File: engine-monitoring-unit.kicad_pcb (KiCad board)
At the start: 2 copper layers, 65.5 x 39.5 mm, 57 parts, among them J1 SW Debug, J2 Supply, J3 Oil Temperature, J4 Air Temperature, J5 Wheel Speed, J7 Inductive Sensor Wire, Q2 MMBT3904, SW1 KEY, SW2 BOOT, SW3 RST, U1 LMR16006XDDCR, U2 STM32F411CEU6, Y1 HSE, Y2 LSE

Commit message: Updated Page Settings, Board Stackup and Constraints
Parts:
- moved D6 109.9 mm to (149.7, 135.2)
- moved C1 109.9 mm to (127.9, 122.2)
- moved C10 109.9 mm to (132.3, 127.2)
- moved C11 109.9 mm to (132.3, 129.7)
- moved C12 109.9 mm to (132.3, 132.3)
- moved C14 109.9 mm to (132.3, 137.3)
- moved C15 109.9 mm to (136.6, 122.2)
- moved C16 109.9 mm to (136.6, 124.7)
- moved C17 109.9 mm to (136.6, 127.2)
- moved C2 109.9 mm to (127.9, 124.7)
- moved C3 109.9 mm to (127.9, 127.2)
- moved C4 109.9 mm to (127.9, 129.7)
- moved C5 109.9 mm to (127.9, 132.3)
- moved C7 109.9 mm to (127.9, 137.3)
- moved C8 109.9 mm to (132.3, 122.2)
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- renumbered D5 to D4, D4 to D5, D7 to D6, D6 to D7, J7 to J6, Q2 to Q1, R16 to R15, R15 to R16
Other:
- board size 65.5 x 39.5 mm -> 70 x 50 mm
- copper layers 2 -> 4

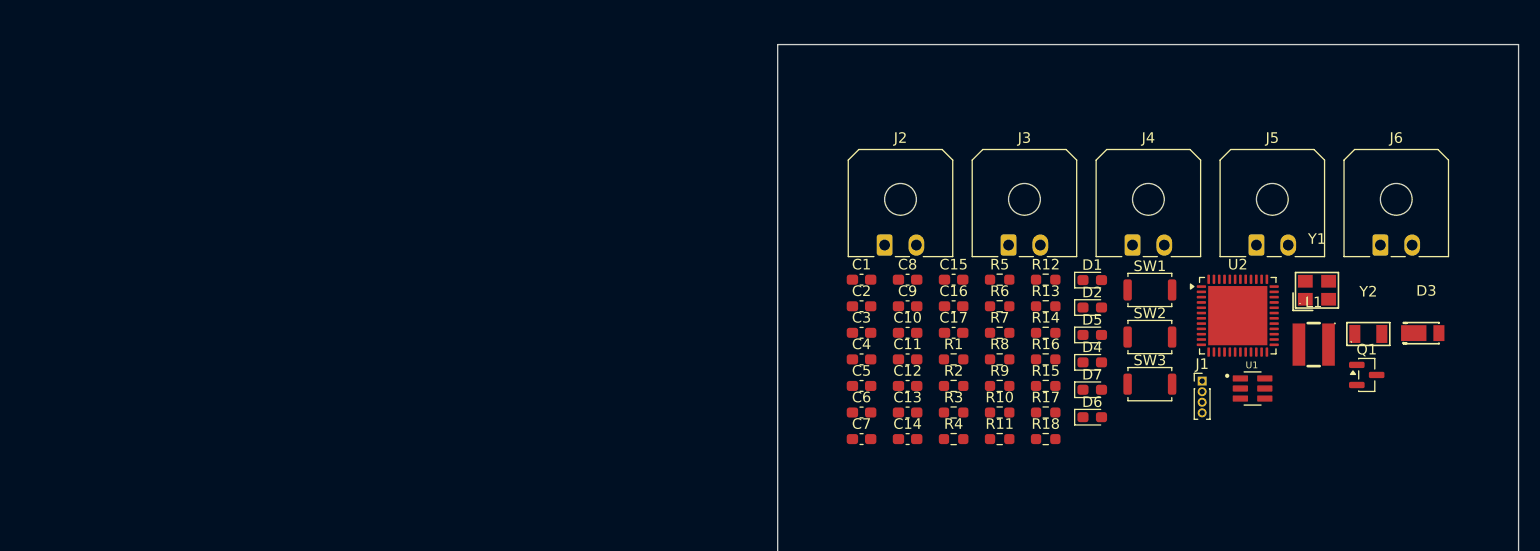
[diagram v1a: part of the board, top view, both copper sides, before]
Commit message: Layed out regulator circuit
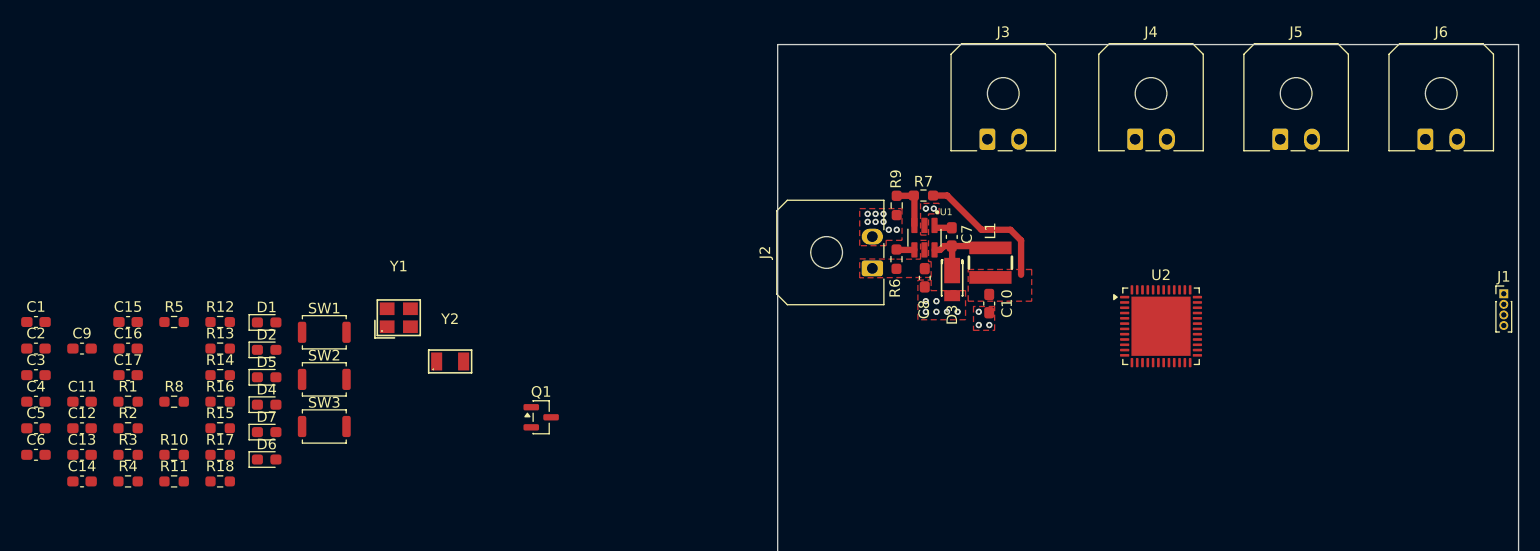
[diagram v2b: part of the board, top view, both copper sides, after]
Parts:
- moved Y2 86.8 mm to (89.1, 129.9)
- moved Y1 86.8 mm to (84.2, 125.8)
- moved C1 78.1 mm to (49.9, 126.2)
- moved C11 78.1 mm to (54.3, 133.7)
- moved C12 78.1 mm to (54.3, 136.3)
- moved C13 78.1 mm to (54.3, 138.8)
- moved C14 78.1 mm to (54.3, 141.3)
- moved C15 78.1 mm to (58.6, 126.2)
- moved C16 78.1 mm to (58.6, 128.7)
- moved C17 78.1 mm to (58.6, 131.2)
- moved C2 78.1 mm to (49.9, 128.7)
- moved C3 78.1 mm to (49.9, 131.2)
- moved C4 78.1 mm to (49.9, 133.7)
- moved C5 78.1 mm to (49.9, 136.3)
- moved C6 78.1 mm to (49.9, 138.8)
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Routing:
- net +3.3V: track 0.00 -> 13.3 mm
- net Net-(D3-K): track 0.00 -> 7.54 mm
- net Net-(U1-FB): track 0.00 -> 4.36 mm
- net Net-(U1-SHDN): track 0.00 -> 1.66 mm
- net Net-(U1-CB): track 0.00 -> 1.41 mm
- net GND: vias 0 -> 19
- added copper zone on F.Cu, net +3.3V
- added copper zone on F.Cu, net GND
- added copper zone on In1.Cu, net GND
- added copper zone on In2.Cu, net GND
- added copper zone on F.Cu, net VIN

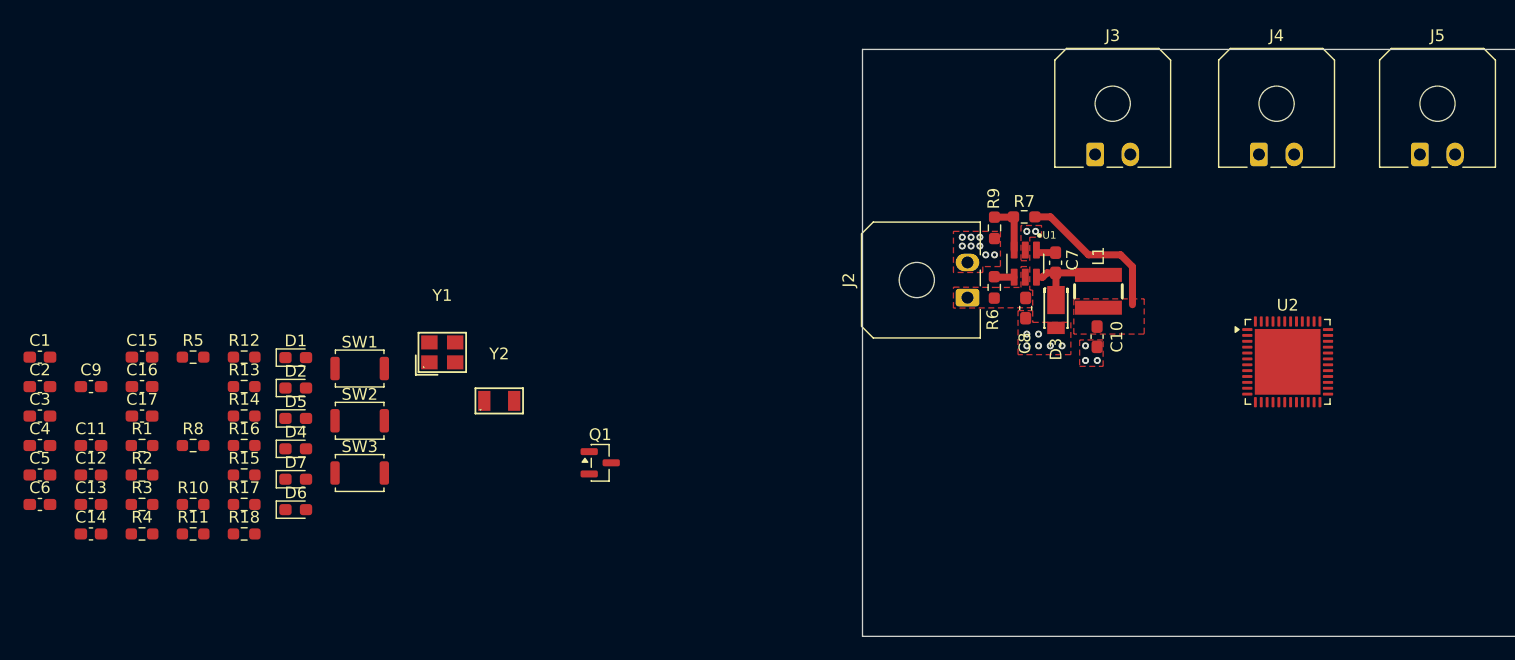
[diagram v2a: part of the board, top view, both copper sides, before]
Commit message: Layed out decoupling caps, connectors and switches
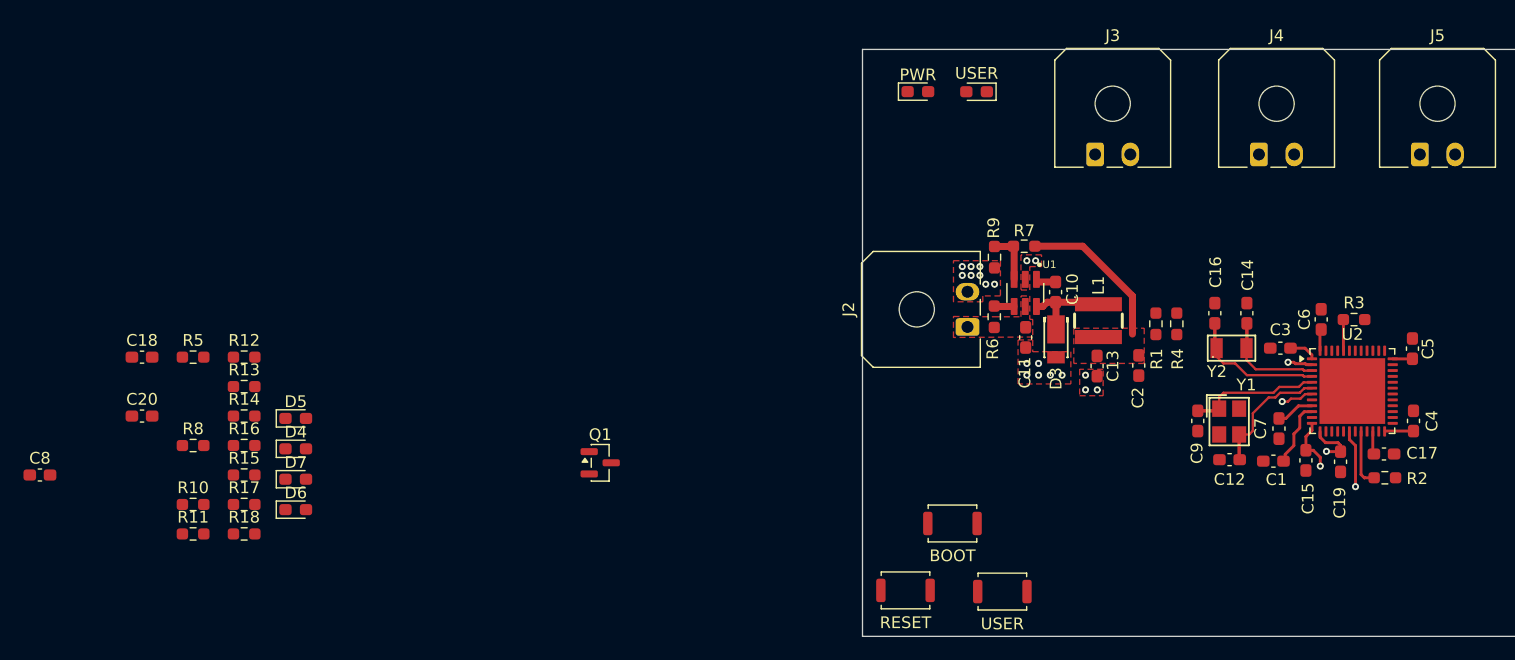
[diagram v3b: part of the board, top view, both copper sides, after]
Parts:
- removed the C14 at (54.3, 141.3)
- added C1: 100nF, Capacitor_SMD:C_0603_1608Metric_Pad1.08x0.95mm_HandSolder, F.Cu at (155.0, 135.1)
- added C17: 4.7uF, Capacitor_SMD:C_0603_1608Metric_Pad1.08x0.95mm_HandSolder, F.Cu at (164.4, 134.5)
- added C6: 100nF, Capacitor_SMD:C_0603_1608Metric_Pad1.08x0.95mm_HandSolder, F.Cu at (159.1, 123.0)
- added C7: 100nF, Capacitor_SMD:C_0603_1608Metric_Pad1.08x0.95mm_HandSolder, F.Cu at (155.5, 132.3)
- moved C5 117.2 mm to (166.8, 125.5), turned to 90 degrees
- moved C4 117.0 mm to (166.9, 131.7), turned to 90 degrees
- moved R2 105.9 mm to (164.5, 136.5)
- moved C3 105.7 mm to (155.6, 125.5), turned to 180 degrees
- moved R3 104.4 mm to (161.9, 123.0)
- moved C15 103.5 mm to (157.8, 135.0), turned to -90 degrees
- moved C19 102.3 mm to (160.7, 135.1), turned to -90 degrees
- moved C14 99.1 mm to (152.7, 122.5), turned to 90 degrees
- moved C9 98.9 mm to (148.6, 131.7), turned to -90 degrees
- moved C12 97.2 mm to (151.3, 134.9), turned to 180 degrees
- moved C16 97.1 mm to (150.0, 122.5), turned to 90 degrees
- moved C2 93.6 mm to (143.5, 126.9), turned to -90 degrees
- moved R4 89.9 mm to (146.8, 123.4), turned to 90 degrees
- moved R1 87.0 mm to (145.0, 123.4), turned to 90 degrees
- moved Y1 67.3 mm to (151.2, 131.7), turned to -90 degrees
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- renumbered SW2 to BOOT, C7 to C10, C8 to C11, C9 to C12, C10 to C13, C11 to C14, C12 to C15, C13 to C16, C15 to C18, C16 to C19, C1 to C2, C17 to C20, C2 to C3, C3 to C4, C4 to C5, C5 to C8, C6 to C9, D2 to PWR, SW3 to RESET, SW1 to USER, D1 to USER
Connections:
- U2 pad 11: /PA1 -> unconnected-(U2-PA1-Pad11)
- U2 pad 13: unconnected-(U2-PA3-Pad13) -> /PA3
- U2 pad 2: unconnected-(U2-PC13-Pad2) -> /PC13
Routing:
- net /PC15: track 0.00 -> 11.5 mm
- net +3.3V: track 13.3 -> 24.7 mm
- net /PH0: track 0.00 -> 11.0 mm
- net /PH1: track 0.00 -> 10.8 mm
- net /PC14: track 0.00 -> 9.04 mm
- net /PA0: track 0.00 -> 5.67 mm
- net /PB0: track 0.00 -> 4.92 mm, vias 0 -> 1
- net /PB2: track 0.00 -> 4.91 mm
- net /PA2: track 0.00 -> 4.73 mm, vias 0 -> 1
- net /PA3: track 0.00 -> 4.27 mm, vias 0 -> 1
- net /NRST: track 0.00 -> 2.80 mm, vias 0 -> 1
- net /BOOT0: track 0.00 -> 2.66 mm
- net /PC13: track 0.00 -> 2.13 mm, vias 0 -> 1
- net /VCAP1: track 0.00 -> 1.92 mm

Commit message: Fixed Schematic Errors
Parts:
- moved R7 0.50 mm to (134.3, 116.8)
- moved R9 0.25 mm to (131.5, 117.7)
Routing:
- net /PA2: track 4.73 -> 7.33 mm
- net +3.3V: track 24.7 -> 24.2 mm
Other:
- board text added: "BATT+"
- board text added: "BATT-"
- board text added: "Engine RPM"
- board text added: "GND"
- board text added: "IAT"
- board text added: "Oil Temp"
- board text added: "SIG"
- board text added: "WHL SPD"
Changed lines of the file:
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@@
 		(tags "capacitor handsolder")
 		(property "Reference" "C15"
-			(at 3.25 -0.18 90)
+			(at 3.785 0.31 180)
 			(layer "F.SilkS")
 			(effects
@@
 	(footprint "Resistor_SMD:R_0603_1608Metric_Pad0.98x0.95mm_HandSolder"
 		(layer "F.Cu")
-		(at 133.775 116.765 180)
+		(at 134.275 116.765 180)
 		(descr "Resistor SMD 0603 (1608 Metric), square (rectangular) end terminal, IPC-7351 nominal with elongated pad for handsoldering. (Body size source: IPC-SM-782 page 72, https://www.pcb-3d.com/wordpress/wp-content/uploads/ipc-sm-782a_amendment_1_and_2.pdf)")
 		(tags "resistor handsolder")
 		(property "Reference" "R7"
-			(at 0 1.32 0)
+			(at 0 1.57 0)
 			(layer "F.SilkS")
 			(effects
@@
 	(footprint "Resistor_SMD:R_0603_1608Metric_Pad0.98x0.95mm_HandSolder"
 		(layer "F.Cu")
-		(at 131.245 117.7 -90)
+		(at 131.495 117.7 -90)
 		(descr "Resistor SMD 0603 (1608 Metric), square (rectangular) end terminal, IPC-7351 nominal with elongated pad for handsoldering. (Body size source: IPC-SM-782 page 72, https://www.pcb-3d.com/wordpress/wp-content/uploads/ipc-sm-782a_amendment_1_and_2.pdf)")
 		(tags "resistor handsolder")
 		(property "Reference" "R9"
-			(at -2.5 0.07 90)
+			(at -2.875 -0.205 270)
 			(layer "F.SilkS")
 			(effects
@@
 		)
 		(embedded_fonts no)
-		(model "${KICAD10_3DMODEL_DIR}/Package_DFN_QFN.3dshapes/QFN-48-1EP_7x7mm_P0.5mm_EP5.6x5.6mm.step"
+		(model "${KIPRJMOD}/ext-libs/STM32F411CEU6/STM32F411CEU6TR.STEP"
 			(offset
 				(xyz 0 0 0)
@@
 			)
 			(rotate
-				(xyz 0 0 0)
+				(xyz -90 -0 -0)
 			)
 		)
@@
 		(layer "Edge.Cuts")
 	)
+	(gr_text "BATT-"
+		(at 123.25 116.25 0)
+		(layer "F.SilkS")
+		(effects
+			(font
+				(size 1 1)
+				(thickness 0.15)
+			)
+			(justify left bottom)
+		)
+	)
+	(gr_text "BATT+\n"
+		(at 123.25 129.25 0)
+		(layer "F.SilkS")
+		(effects
+			(font
+				(size 1 1)
+				(thickness 0.15)
+			)
+			(justify left bottom)
+		)
+	)
+	(gr_text "SIG\n"
+		(at 136.5 112 0)
+		(layer "F.SilkS")
+		(effects
+			(font
+				(size 1 1)
+				(thickness 0.15)
+			)
+			(justify left bottom)
+		)
+	)
+	(gr_text "GND"
+		(at 143 112 0)
+		(layer "F.SilkS")
+		(effects
+			(font
+				(size 1 1)
+				(thickness 0.15)
+			)
+			(justify left bottom)
+		)
+	)
+	(gr_text "SIG\n"
+		(at 150.25 112.25 0)
+		(layer "F.SilkS")
+		(effects
+			(font
+				(size 1 1)
+				(thickness 0.15)
+			)
+			(justify left bottom)
+		)
+	)
+	(gr_text "GND"
+		(at 156.75 112.25 0)
+		(layer "F.SilkS")
+		(effects
+			(font
+				(size 1 1)
+				(thickness 0.15)
+			)
+			(justify left bottom)
+		)
+	)
+	(gr_text "SIG\n"
+		(at 164 112.25 0)
+		(layer "F.SilkS")
+		(effects
+			(font
+				(size 1 1)
+				(thickness 0.15)
+			)
+			(justify left bottom)
+		)
+	)
+	(gr_text "GND"
+		(at 170.5 112.25 0)
+		(layer "F.SilkS")
+		(effects
+			(font
+				(size 1 1)
+				(thickness 0.15)
+			)
+			(justify left bottom)
+		)
+	)
+	(gr_text "SIG\n"
+		(at 178 112.25 0)
+		(layer "F.SilkS")
+		(effects
+			(font
+				(size 1 1)
+				(thickness 0.15)
+			)
+			(justify left bottom)
+		)
+	)
+	(gr_text "GND"
+		(at 184.5 112.25 0)
+		(layer "F.SilkS")
+		(effects
+			(font
+				(size 1 1)
+				(thickness 0.15)
+			)
+			(justify left bottom)
+		)
+	)
+	(gr_text "Oil Temp\n"
+		(at 137 114 0)
+		(layer "F.SilkS")
+		(effects
+			(font
+				(size 1.2 1.2)
+				(thickness 0.2)
+				(bold yes)
+			)
+			(justify left bottom)
+		)
+	)
+	(gr_text "IAT\n"
+		(at 153.5 114.25 0)
+		(layer "F.SilkS")
+		(effects
+			(font
+				(size 1.2 1.2)
+				(thickness 0.2)
+				(bold yes)
+			)
+			(justify left bottom)
+		)
+	)
+	(gr_text "WHL SPD\n"
+		(at 164.75 114.5 0)
+		(layer "F.SilkS")
+		(effects
+			(font
+				(size 1.2 1.2)
+				(thickness 0.2)
+				(bold yes)
+			)
+			(justify left bottom)
+		)
+	)
+	(gr_text "Engine RPM\n"
+		(at 177.25 114.5 0)
+		(layer "F.SilkS")
+		(effects
+			(font
+				(size 1.2 1.2)
+				(thickness 0.2)
+				(bold yes)
+			)
+			(justify left bottom)
+		)
+	)
 	(via
 		(at 130 118.5)
@@
 	)
 	(via
-		(at 134 118)
+		(at 134 118.25)
 		(size 0.6)
 		(drill 0.3)
@@
 	)
 	(via
-		(at 134.75 118)
+		(at 134.75 118.25)
 		(size 0.6)
 		(drill 0.3)
@@
 	)
 	(segment
-		(start 134.6875 116.765)
-		(end 138.756 116.765)
-		(width 0.6)
-		(layer "F.Cu")
-		(net "+3.3V")
-	)
-	(segment
 		(start 165.1575 126.365)
 		(end 166.8375 126.365)
@@
 	)
 	(segment
+		(start 135.1875 116.765)
+		(end 138.756 116.765)
+		(width 0.6)
+		(layer "F.Cu")
+		(net "+3.3V")
+	)
+	(segment
 		(start 158.2825 126.0325)
 		(end 157.7 125.45)
@@
 	)
 	(segment
-		(start 159 134.75)
-		(end 159 135.5)
+		(start 158.25 137.5)
+		(end 158.75 137)
 		(width 0.25)
 		(layer "F.Cu")
@@
 	)
 	(segment
-		(start 157.775 132.975)
-		(end 158.2925 132.4575)
+		(start 158.75 137)
+		(end 158.75 134.5)
 		(width 0.25)
 		(layer "F.Cu")
@@
 	(segment
 		(start 158.3975 134.1475)
-		(end 159 134.75)
+		(end 157.775 134.1475)
 		(width 0.25)
 		(layer "F.Cu")
@@
 	)
 	(segment
-		(start 157.775 134.1475)
-		(end 157.775 132.975)
+		(start 157.75 137.5)
+		(end 158.25 137.5)
 		(width 0.25)
 		(layer "F.Cu")
@@
 	)
 	(segment
-		(start 157.775 134.1475)
+		(start 158.75 134.5)
 		(end 158.3975 134.1475)
 		(width 0.25)
@@
 		(net "/PA2")
 	)
+	(segment
+		(start 157.775 132.975)
+		(end 158.2925 132.4575)
+		(width 0.25)
+		(layer "F.Cu")
+		(net "/PA2")
+	)
+	(segment
+		(start 157.775 134.1475)
+		(end 157.775 132.975)
+		(width 0.25)
+		(layer "F.Cu")
+		(net "/PA2")
+	)
 	(via
-		(at 159 135.5)
+		(at 157.75 137.5)
 		(size 0.6)
 		(drill 0.3)
@@
 	)
 	(segment
-		(start 132.92 119.59)
-		(end 132.92 116.8225)
+		(start 132.92 117.83)
+		(end 132.92 119.59)
+		(width 0.6)
+		(layer "F.Cu")
+		(net "Net-(U1-FB)")
+	)
+	(segment
+		(start 133.3625 116.765)
+		(end 133.3625 117.3875)
+		(width 0.6)
+		(layer "F.Cu")
+		(net "Net-(U1-FB)")
+	)
+	(segment
+		(start 131.495 116.7875)
+		(end 133.34 116.7875)
 		(width 0.6)
 		(layer "F.Cu")
@@
 	)
 	(segment
-		(start 131.245 116.7875)
-		(end 132.84 116.7875)
+		(start 133.3625 117.3875)
+		(end 132.92 117.83)
 		(width 0.6)
 		(layer "F.Cu")
@@
 		(polygon
 			(pts
-				(xy 133.5 120.5) (xy 134.25 120.5) (xy 134.25 118.5) (xy 135.25 118.5) (xy 135.25 117.5) (xy 133.5 117.5)
+				(xy 133.5 120.5) (xy 134.25 120.5) (xy 134.25 118.5) (xy 135.25 118.5) (xy 135.25 117.75) (xy 133.5 117.75)
 			)
 		)
